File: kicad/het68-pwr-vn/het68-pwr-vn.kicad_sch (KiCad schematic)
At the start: 61 parts, among them J1 CT_SEC, J2 USB_C, J3 VOUT, Q1 X0202MN, Q2 AO3400A, Q3 AO3401A, Q4 AO3400A

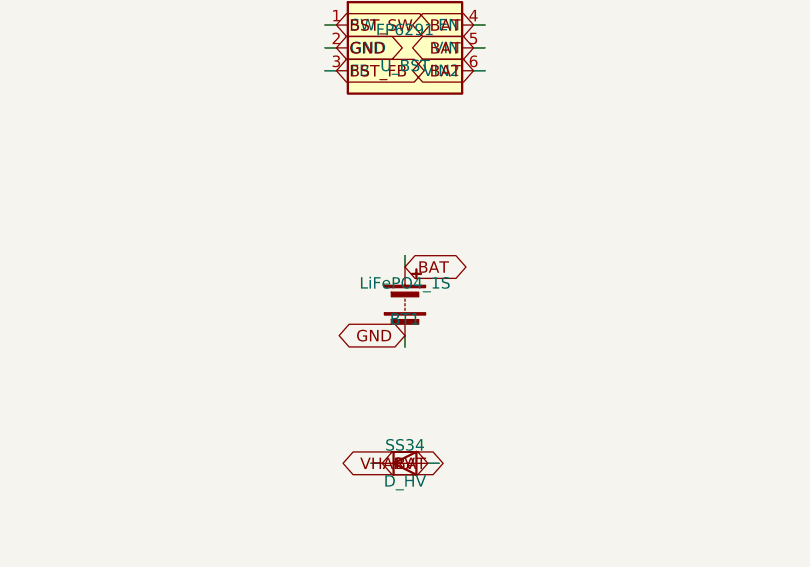
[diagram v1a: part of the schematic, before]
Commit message: Add a Core status LED and three buttons, and fit a 21700 holder.
RESET, BOOT and USER sit on the east edge with one SK6812; the power board uses a Keystone 1122 instead of an 18650 sled. Masks, schematics and JLCPCB gerber zips are in the tree.

Co-authored-by: Cursor <cursoragent@cursor.com>
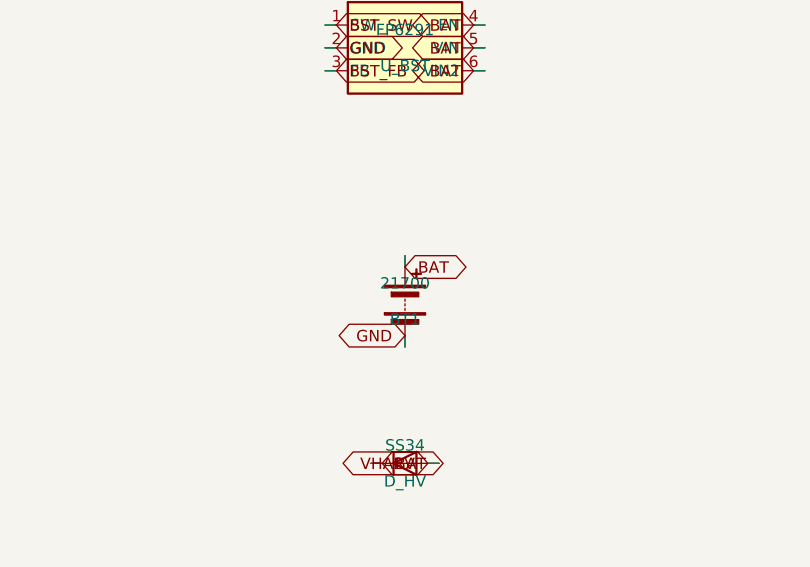
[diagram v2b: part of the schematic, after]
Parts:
- BT1: value LiFePO4_1S -> 21700; footprint Battery:BatteryHolder_Keystone_1042_1x18650 -> het68:Keystone_1122_21700; MPN LiFePO4 / LTO 1S -> Keystone 1122
